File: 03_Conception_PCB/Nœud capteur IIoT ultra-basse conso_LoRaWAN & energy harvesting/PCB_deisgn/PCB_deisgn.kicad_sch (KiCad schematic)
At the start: 24 parts, among them J1 SWD1, U1 AEM10941-QFN, U2 STM32U073C8Ux, Y1 Crystal

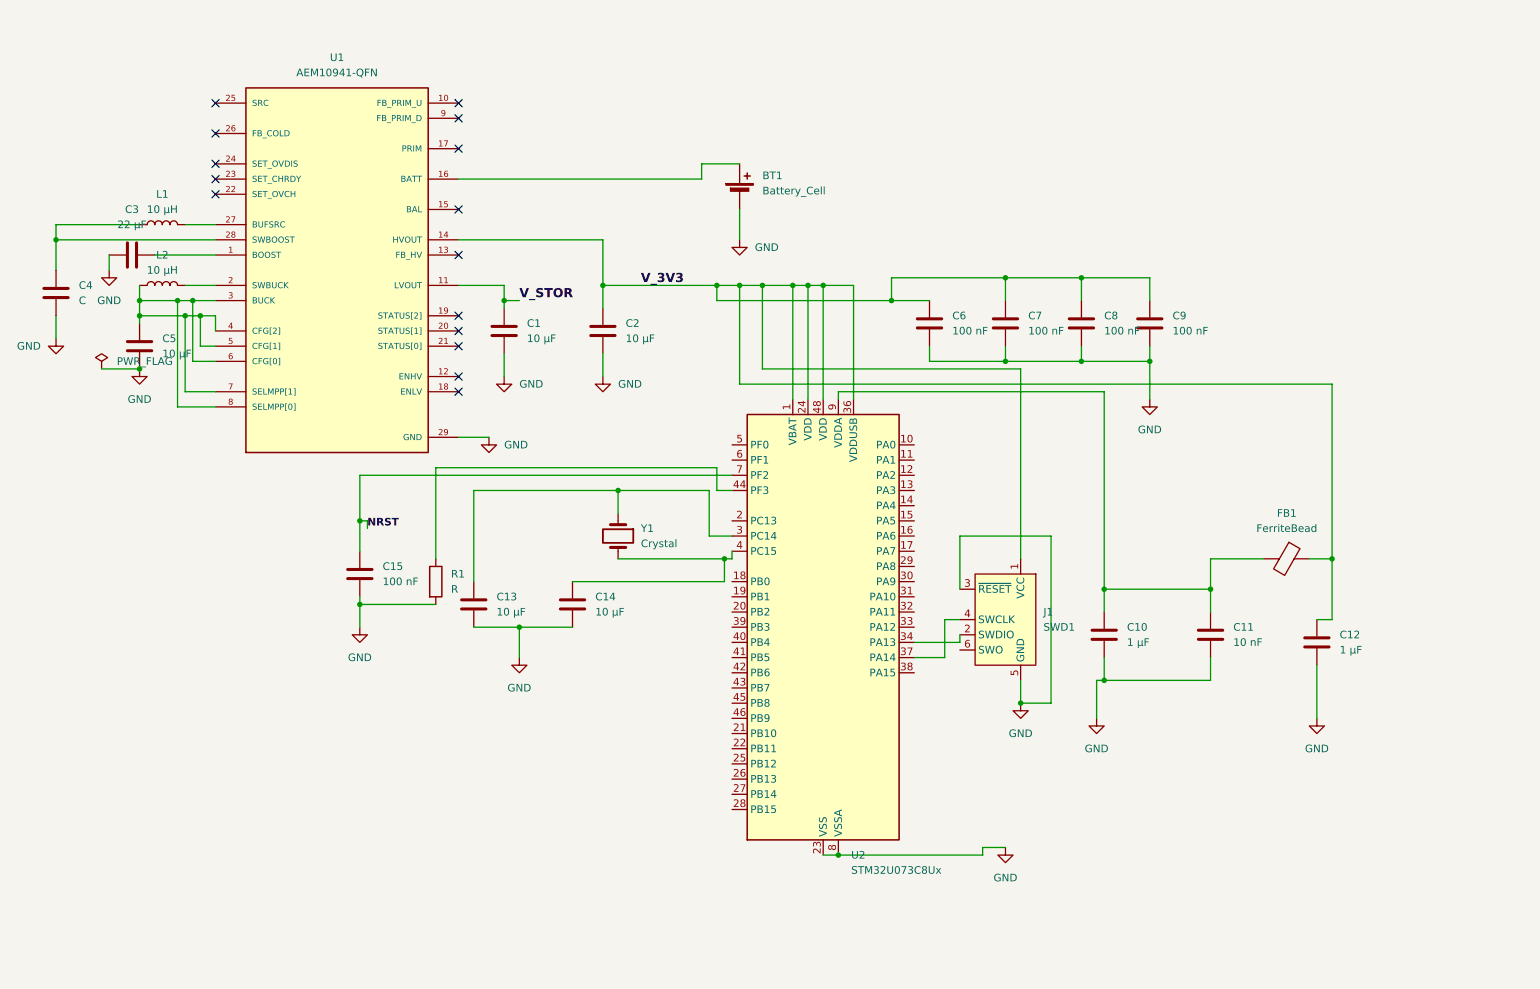
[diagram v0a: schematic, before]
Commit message: fix(sch): disconnect NRST from GND (was holding mcu in reset) fix(sch): wire SWD reset to mcu NRST net feat(sch): add 10k pullup on NRST fix(sch): connect SWD VCC to mcu supply rail docs(sch): record clean ERC run for mcu block
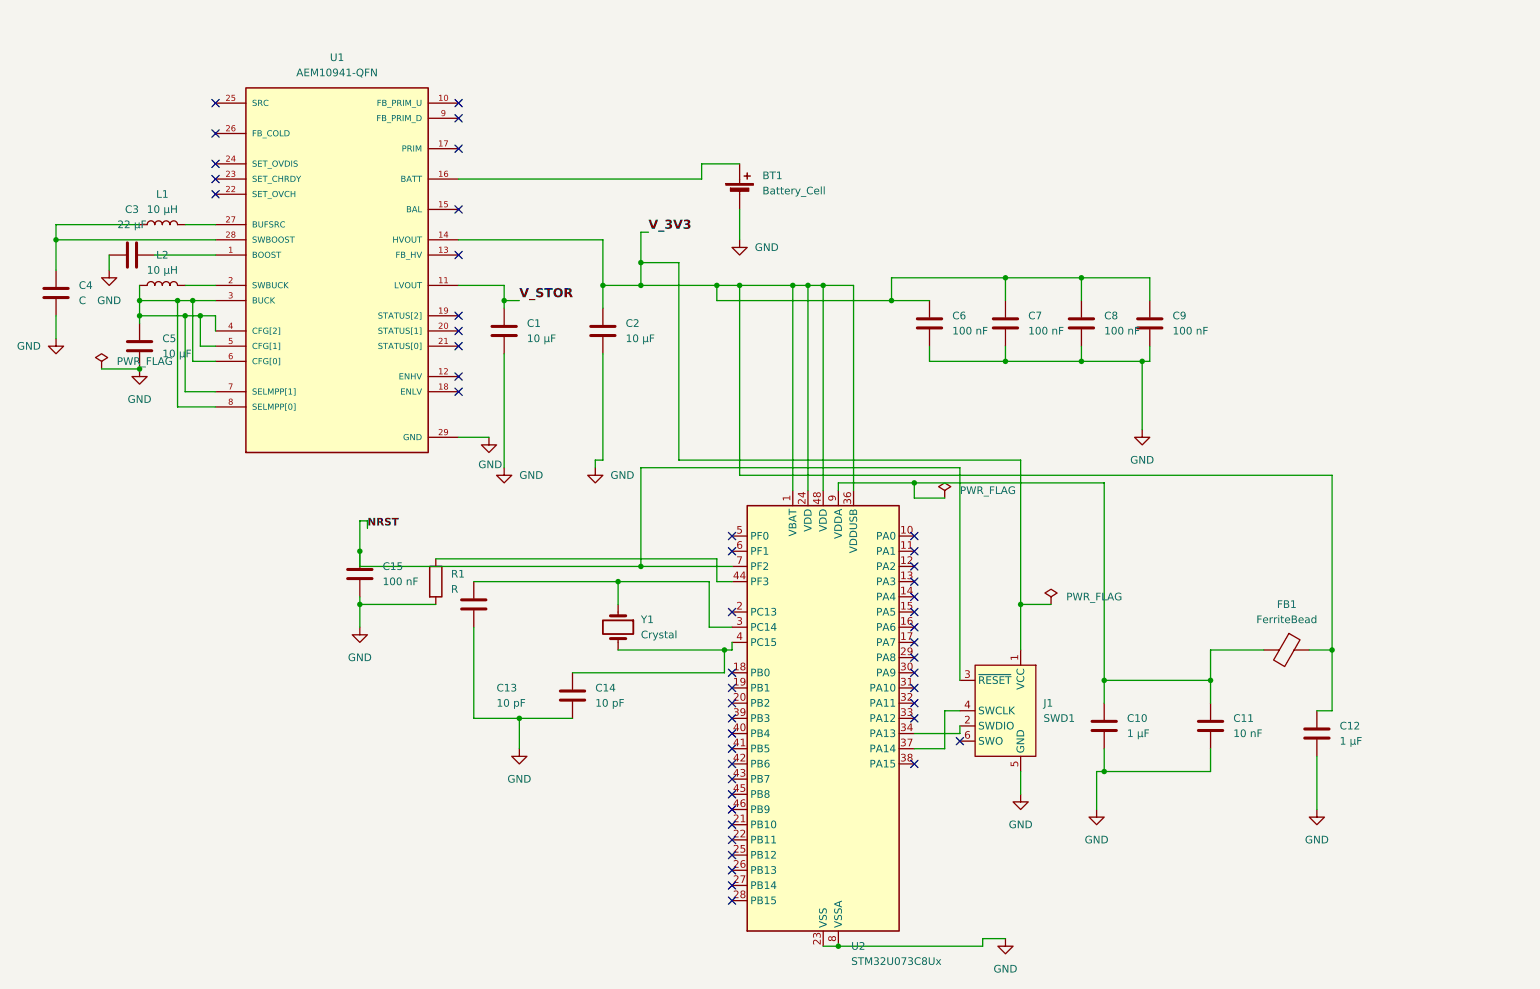
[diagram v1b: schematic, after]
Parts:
- C13, C14: value 10 µF -> 10 pF
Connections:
- net GND: no longer J1.3 (~{RESET})
- net NRST: now also J1.3 (~{RESET})
- no-connect marks 15 -> 49
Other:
- moved on the sheet: C10, C11, C12, C14, FB1, J1, U2, Y1

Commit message: UPDATE
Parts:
- removed C15: 100 nF, symbol Device:C
- removed R1: R, symbol Device:R
- C10, C12: value 1 µF -> C
- C11: value 10 nF -> C
- C13, C14: value 10 pF -> C
- C6, C7, C8, C9: value 100 nF -> C
- FB1: footprint (none) -> Inductor_SMD:L_6.3x6.3_H3
- J1: value SWD1 -> SWD
- Y1: footprint Crystal:Crystal_AT310_D3.0mm_L10.0mm_Horizontal -> (none)
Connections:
- net GND: no longer U2.23 (VSS), U2.35 (VSS), U2.47 (VSS), U2.49 (VSS), U2.8 (VSSA)
- net V_3V3: no longer C12.1, C6.1, C7.1, C8.1, C9.1, FB1.1, J1.1 (VCC), U2.1 (VBAT), U2.24 (VDD), U2.36 (VDDUSB), U2.48 (VDD)
- net at C10.1, C11.1, U2.9 (VDDA): no longer FB1.2
- net at J1.2 (SWDIO): no longer U2.34 (PA13)
- net at J1.4 (SWCLK): no longer U2.37 (PA14)
- net at C13.1, Y1.1: now also U2.4 (PC15); no longer U2.3 (PC14)
- net NRST: no longer names the net of U2.7 (PF2)
- net NRST: now also C14.1; no longer J1.3 (~{RESET})
- new net: C6.1, C7.1, C8.1, C9.1, FB1.2, U2.1 (VBAT), U2.24 (VDD), U2.36 (VDDUSB), U2.48 (VDD)
- new net: C12.1, U2.3 (PC14), Y1.2
- new net: U2.23 (VSS), U2.35 (VSS), U2.47 (VSS), U2.49 (VSS)
- no-connect marks 49 -> 15
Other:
- moved on the sheet: BT1

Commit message: add robotics project files
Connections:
- net GND: now also U1.10 (FB_PRIM_U), U1.15 (BAL), U1.9 (FB_PRIM_D)
- no-connect marks 15 -> 57
